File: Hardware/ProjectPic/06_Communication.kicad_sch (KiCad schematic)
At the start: 22 parts, among them J10 SPI_5V_Headers, J11 IMU_Headers, J12 Micro_SD_Card_Det1, J13 PWM_Headers, J14 Servo_headers, J15 I2C_3V3_Headers, J16 SPI_3V3_Headers, J8 UART_Headers, J9 I2C_5V_Headers, U5 W25Q128JVS

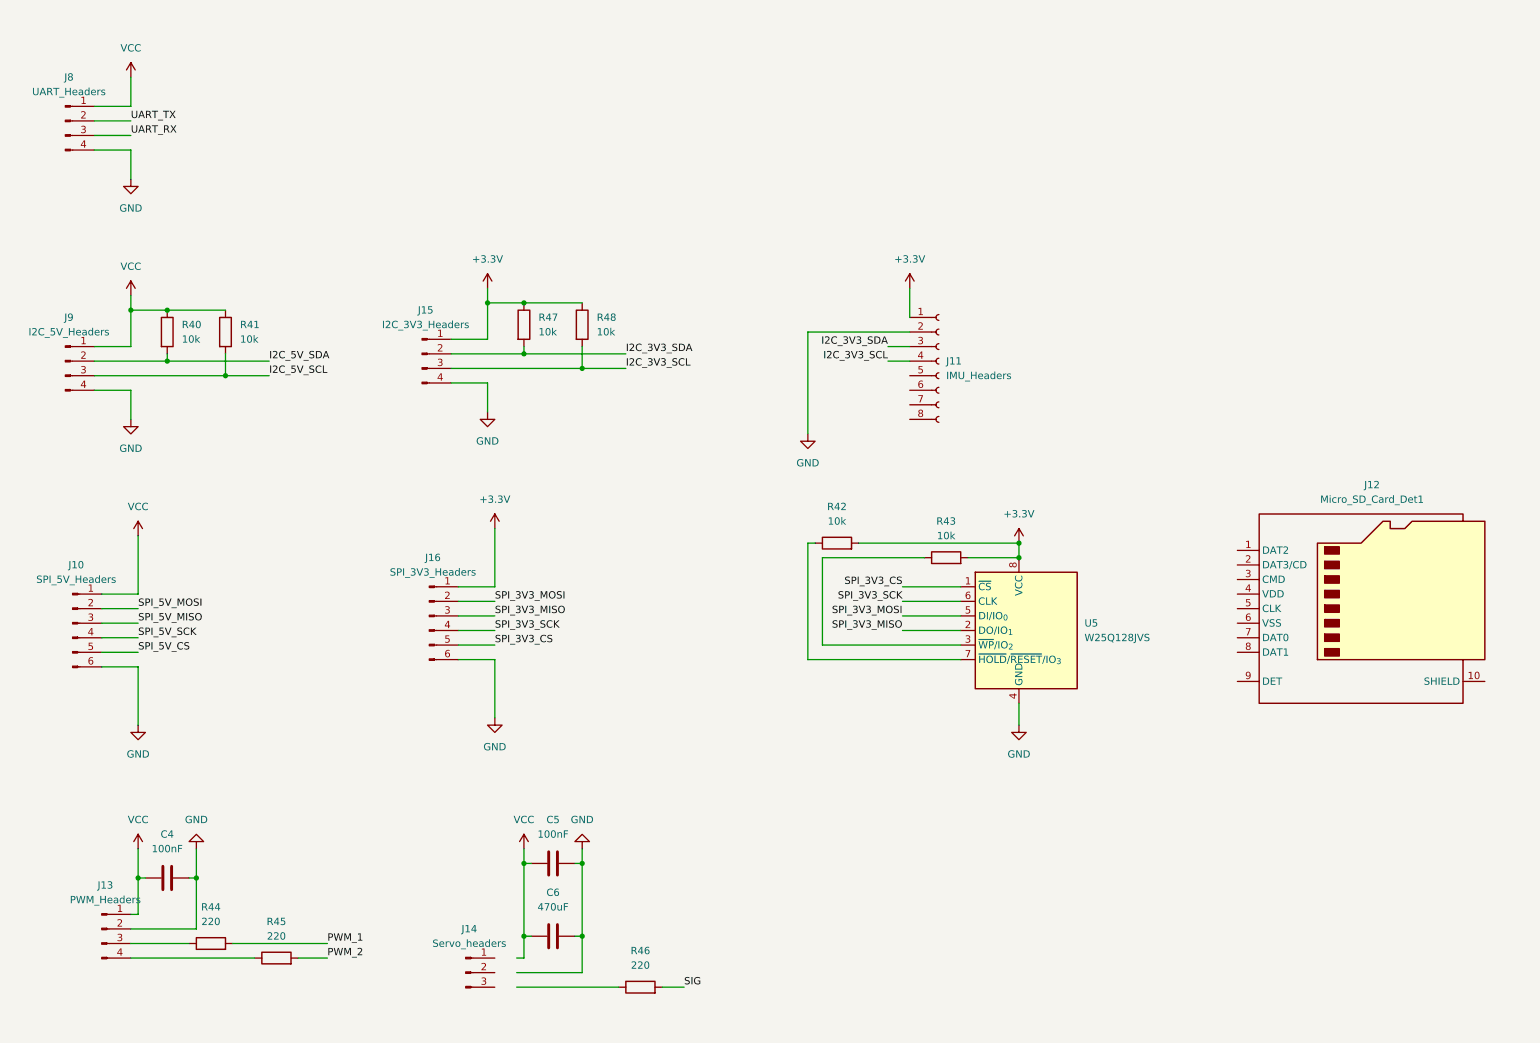
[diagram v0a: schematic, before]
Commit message: Port C: component support incresed
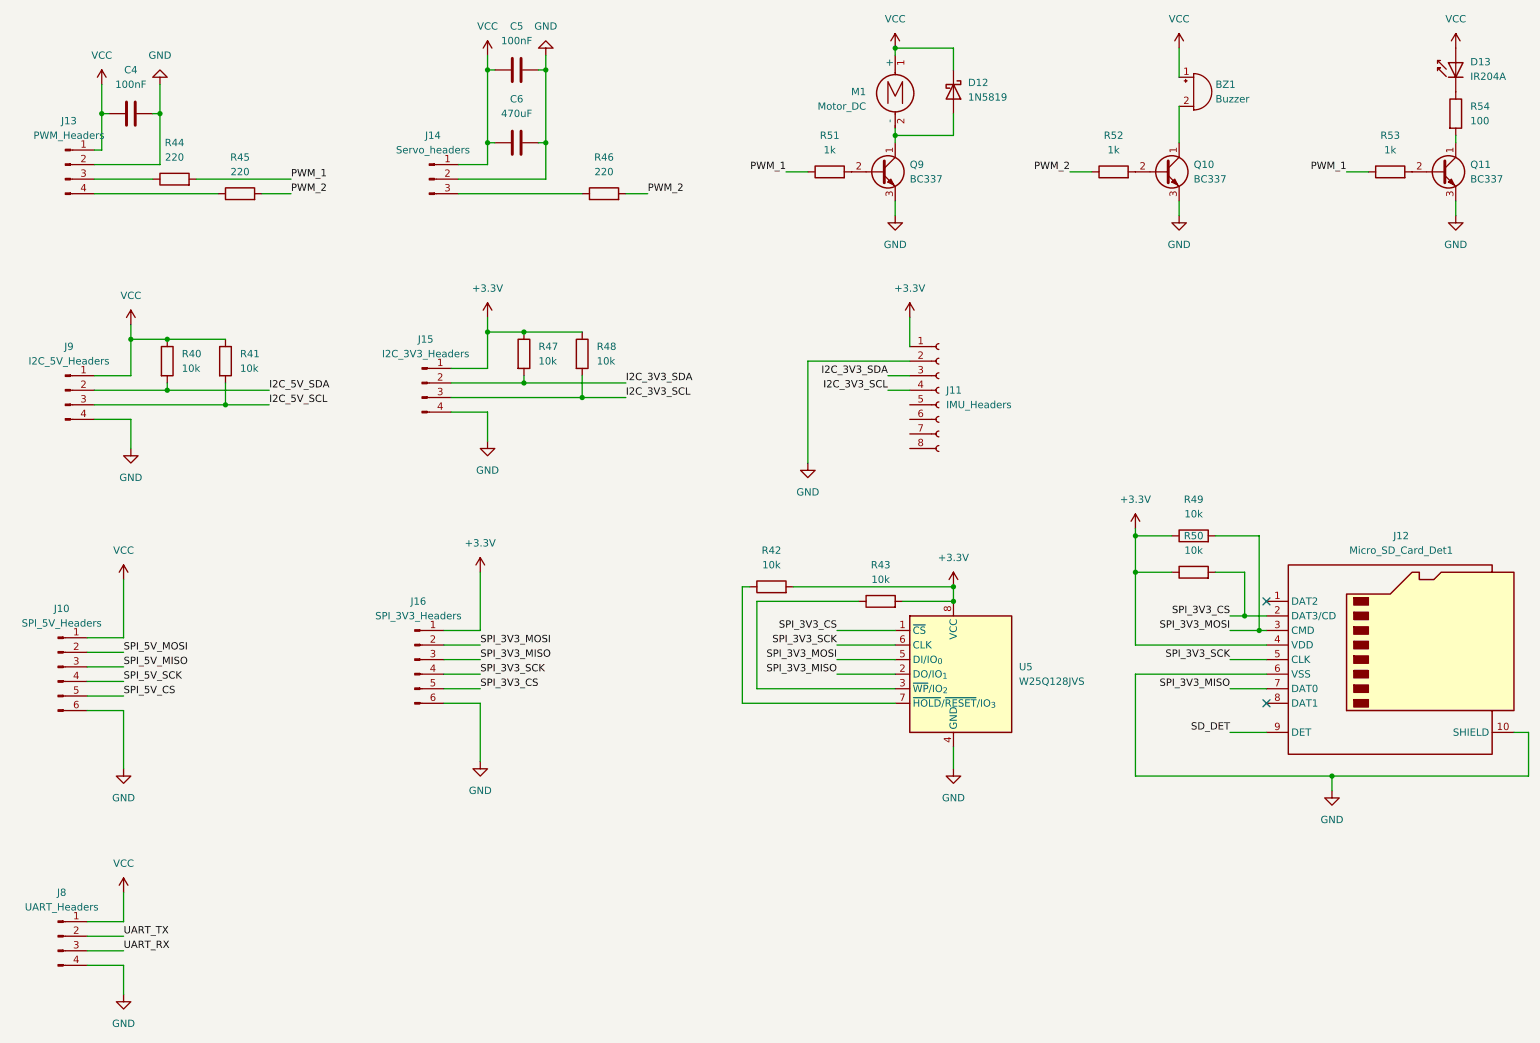
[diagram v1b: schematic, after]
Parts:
- added BZ1: Buzzer, symbol Device:Buzzer
- added D12: 1N5819, Diode_THT:D_DO-41_SOD81_P10.16mm_Horizontal, symbol Diode:1N5819
- added D13: IR204A, LED_THT:LED_D3.0mm_IRBlack, symbol LED:IR204A
- added M1: Motor_DC, symbol Motor:Motor_DC
- added Q10, Q11, Q9: BC337, Package_TO_SOT_THT:TO-92_Inline, symbol Transistor_BJT:BC337
- added R49, R50: 10k, symbol Device:R
- added R51, R52, R53: 1k, symbol Device:R
- added R54: 100, symbol Device:R
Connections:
- net SIG is gone; now on net PWM_2: R46.2
- net +3.3V: now also J12.4 (VDD), R49.1, R50.1
- net GND: now also J12.10 (SHIELD), J12.6 (VSS), J14.2 (Pin_2), Q10.3 (E), Q11.3 (E), Q9.3 (E)
- net PWM_1: now also R51.1, R53.1
- net PWM_2: now also R52.1
- net SPI_3V3_CS: now also J12.2 (DAT3/CD), R50.2
- net SPI_3V3_MISO: now also J12.7 (DAT0)
- net SPI_3V3_MOSI: now also J12.3 (CMD), R49.2
- net SPI_3V3_SCK: now also J12.5 (CLK)
- net VCC: now also J14.1 (Pin_1), BZ1.1 (+), D12.1 (K), D13.2 (A), M1.1 (+)
- net at J14.3 (Pin_3): now also R46.1
- net SD_DET: now reaches J12.9 (DET)
- new net: D12.2 (A), M1.2 (-), Q9.1 (C)
- new net: Q9.2 (B), R51.2
- new net: Q10.2 (B), R52.2
- new net: BZ1.2 (-), Q10.1 (C)
- new net: Q11.1 (C), R54.2
- new net: Q11.2 (B), R53.2
- new net: D13.1 (K), R54.1
- no-connect marks 0 -> 2
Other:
- moved on the sheet: C4, C5, C6, J10, J11, J12, J13, J14, J15, J16, J8, J9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
